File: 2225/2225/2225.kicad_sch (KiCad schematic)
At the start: 2 parts, among them T1 Transformer_1P_SS

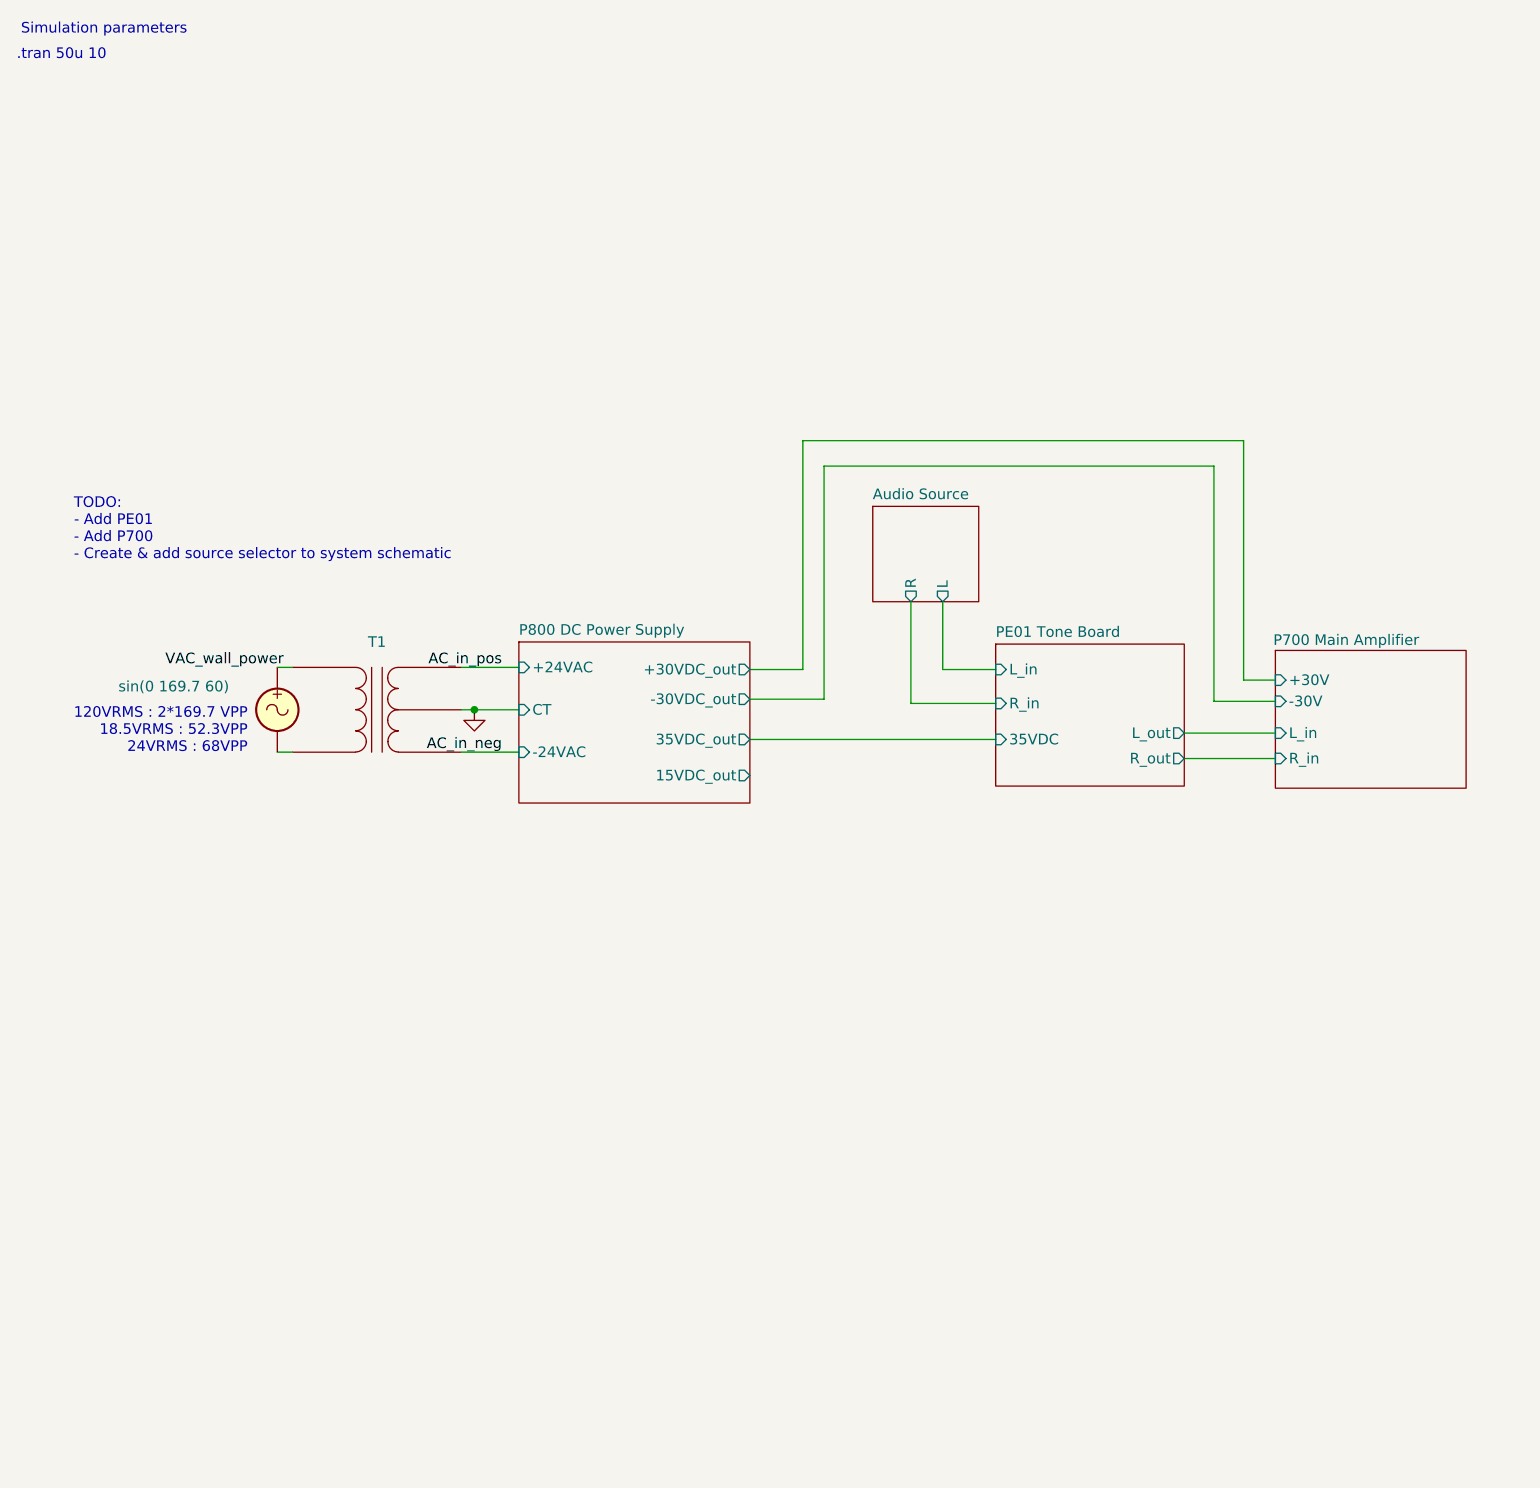
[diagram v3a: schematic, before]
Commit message: Initial system block diagram of 2225
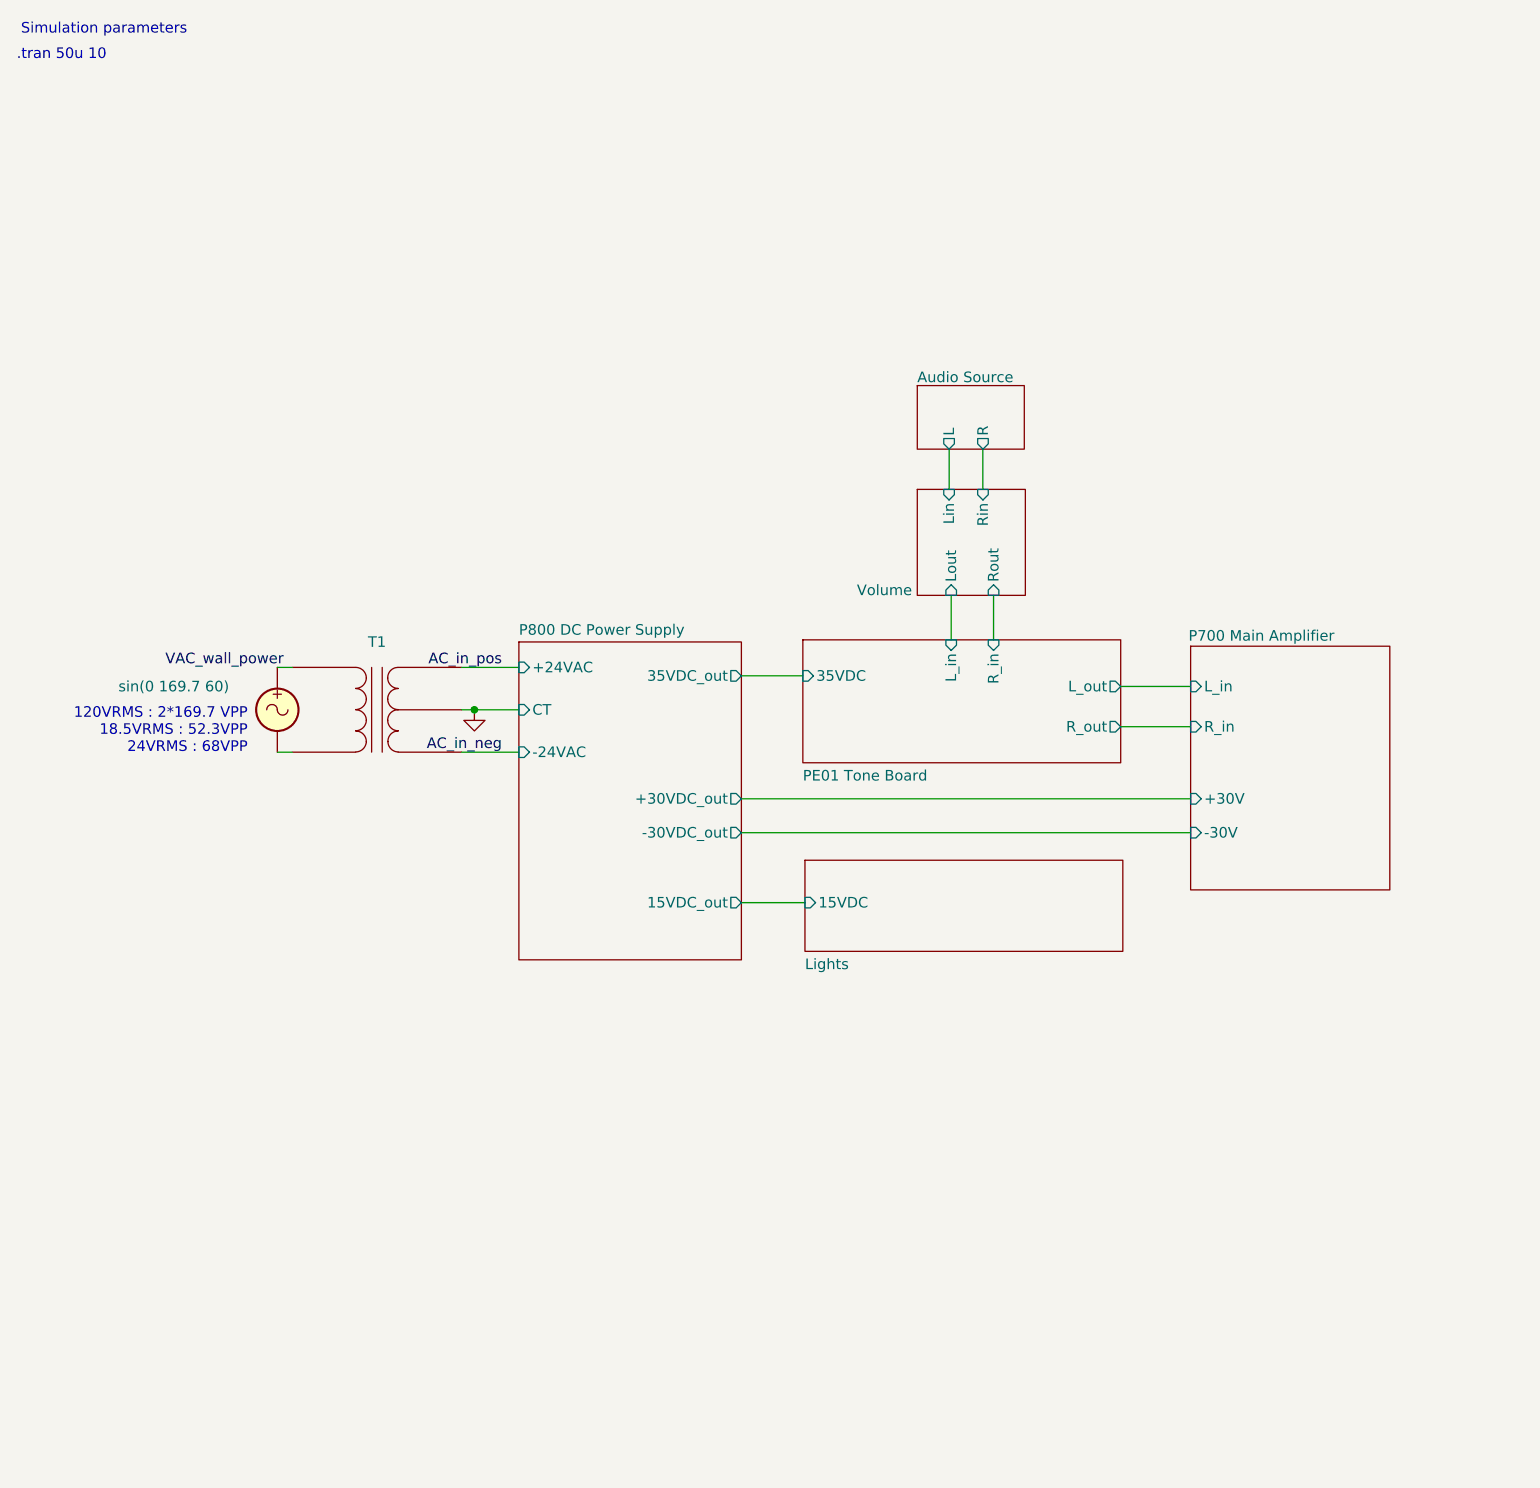
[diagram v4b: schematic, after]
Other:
- added sheet Lights (lights.kicad_sch)
- added sheet Volume (volume.kicad_sch)
- note removed: "TODO: - Add PE01 - Add P700 - Create & add source selector to system schematic"
